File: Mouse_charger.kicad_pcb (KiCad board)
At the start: 2 copper layers, 48 x 10.4 mm, 17 parts, among them CON1 AAA_Bat_PC_con, CON2 Molex_105133-0011, CON3 1.5mm_PTH, CON4 AAA_Bat_PC_con, U1 MCP73831-2ACI/OT, U2 MCP1700-3002E/MB

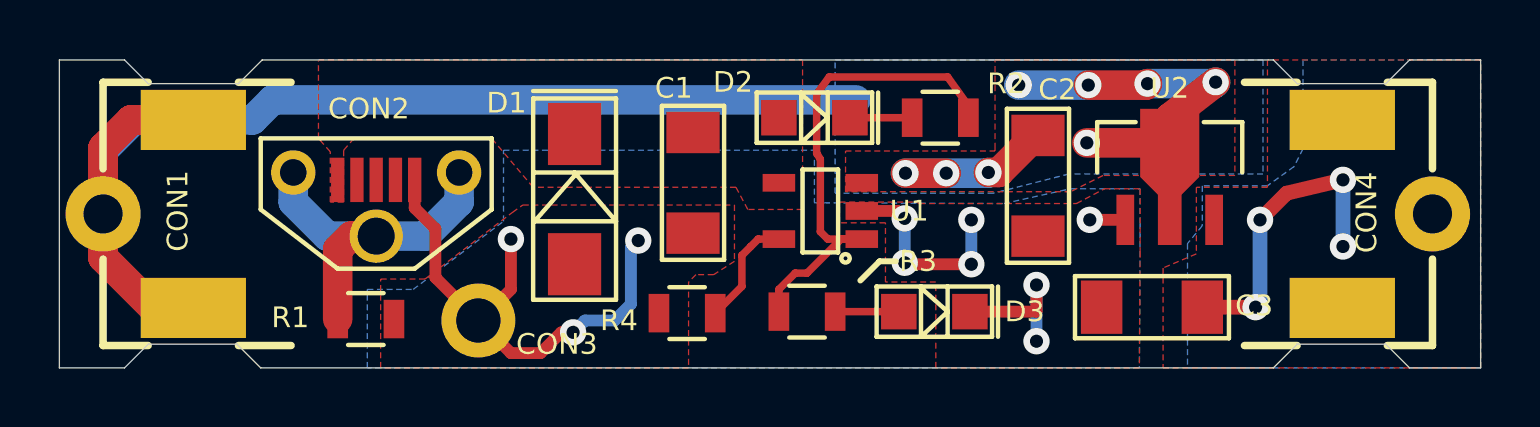
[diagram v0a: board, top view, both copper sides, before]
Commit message: Added V_bus plane on bottom
Added V_bus plane on bottom for better U1 heat dissipation
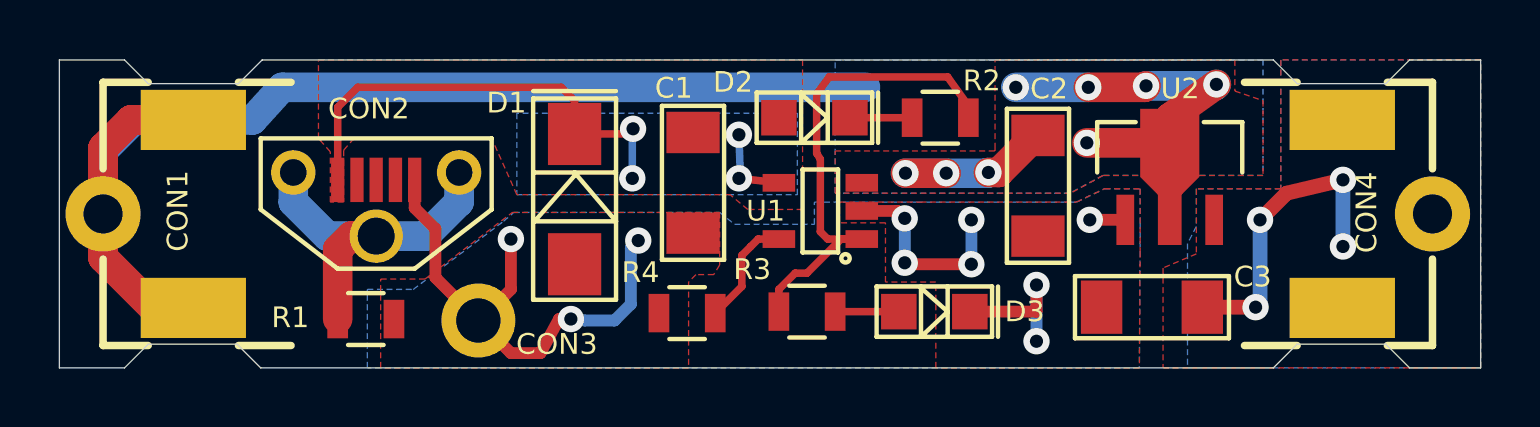
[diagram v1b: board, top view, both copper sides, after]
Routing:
- net /V_bus: track 0.00 -> 18.7 mm, vias 0 -> 4
- net /V_batt: track 75.2 -> 75.8 mm
- added copper zone on B.Cu, net /V_bus
